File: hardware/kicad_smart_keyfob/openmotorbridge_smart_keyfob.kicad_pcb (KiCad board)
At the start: 2 copper layers, 38 x 19 mm, 25 parts, among them M1 LRA_MOTOR_PADS, SW1 BTN_ARM, SW2 BTN_SOS, U1 nRF52840-QIAA, U2 SX1262IMLTRT, U3 DRV2605LDGSR, U4 BQ51003YFPR, U5 BQ25100YFPR, Y1 32.000MHz, Y2 32.768kHz, Y3 32MHz_TCXO

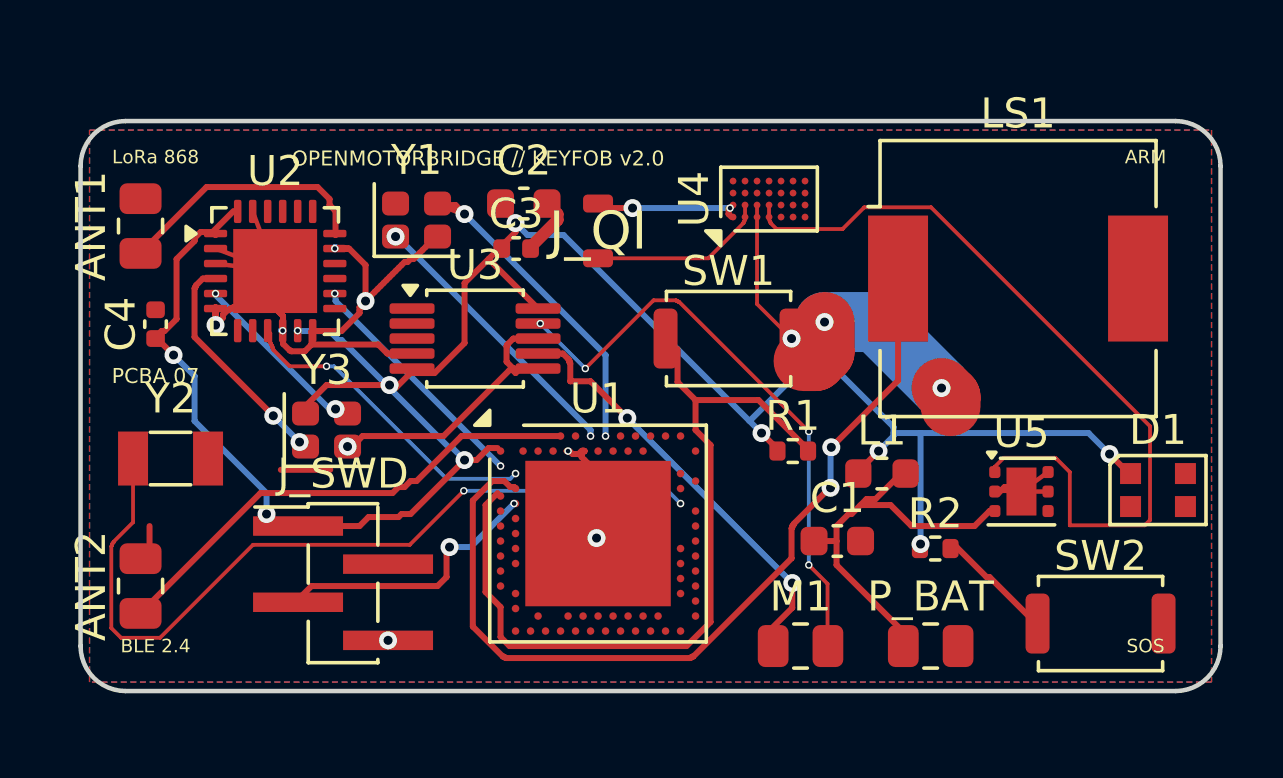
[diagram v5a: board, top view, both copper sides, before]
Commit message: hardware(pcba): commit user manual routing updates for PCBA 07 (keyfob) and PCBA 08 (radar)
- PCBA 07 (Smart Keyfob): 0 unconnected items, complete manual routing of nRF52840, SX1262, Qi charging and power circuits
- PCBA 08 (Radar Sub-MCU): 0 unconnected items, 0 clearance/shorting errors, complete manual routing of MR20 radar interface (TX/RX), ESP32-C5 and power
- Updated high-resolution 3D renders for both boards in hardware/ and docs/images/pcba/
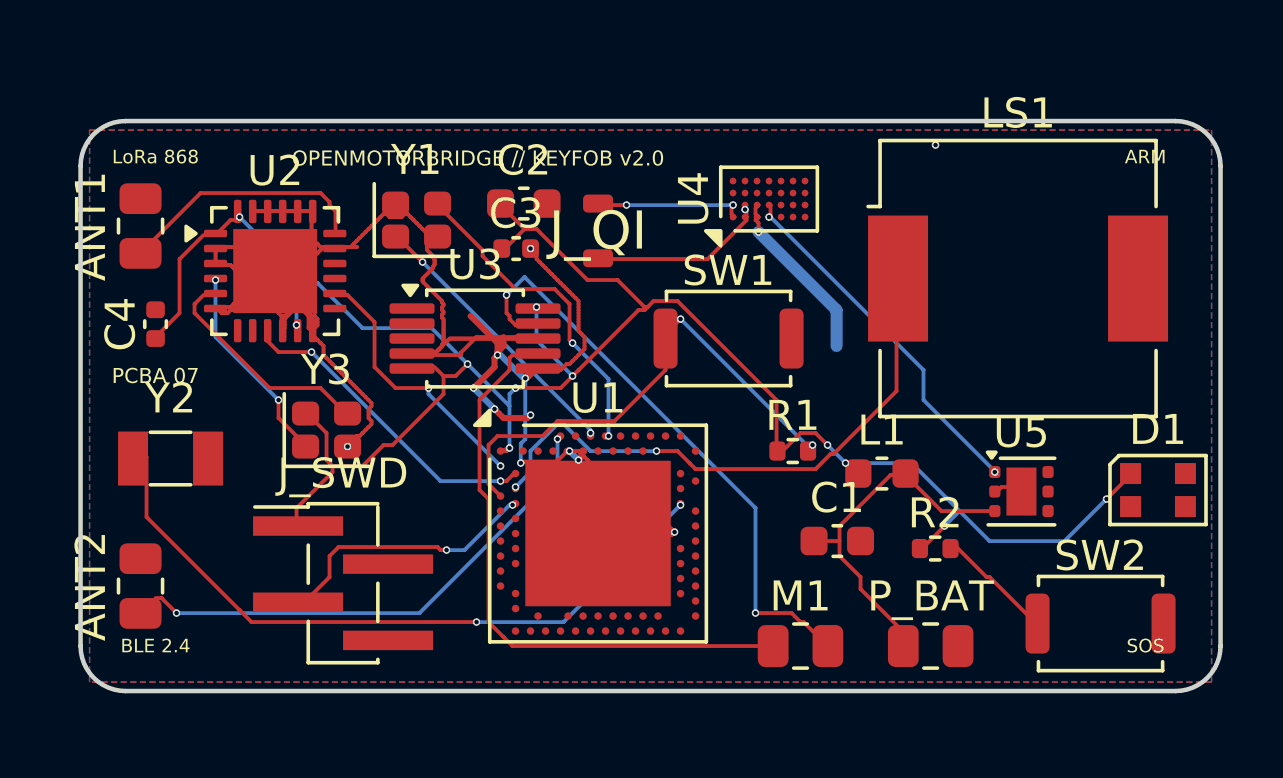
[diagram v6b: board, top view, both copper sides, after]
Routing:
- net GND: track 60.5 -> 88.5 mm, vias 11 -> 13
- net VCC_QI_5V: track 27.3 -> 12.1 mm, vias 0 -> 2
- net BUZZER_PWM: track 29.2 -> 19.6 mm
- net BTN_ARM_N: track 26.7 -> 17.2 mm, vias 0 -> 2
- net LRA_POS: track 14.6 -> 20.2 mm, vias 2 -> 0
- net RTC2: track 27.3 -> 23.3 mm
- net VCC_3V3: track 75.6 -> 73.4 mm, vias 10 -> 11
- net VBAT: track 13.9 -> 12.4 mm
- net TCXO_OUT: track 6.11 -> 7.33 mm, vias 2 -> 0
- net LORA_SCK: track 7.98 -> 8.91 mm
- net TCXO_IN: track 7.65 -> 6.84 mm
- net BLE_ANT_50R: track 16.4 -> 16.9 mm, vias 0 -> 2
- net QI_AC2: track 5.92 -> 6.25 mm, vias 0 -> 1
- net LRA_NEG: track 19.8 -> 20.0 mm, vias 4 -> 2

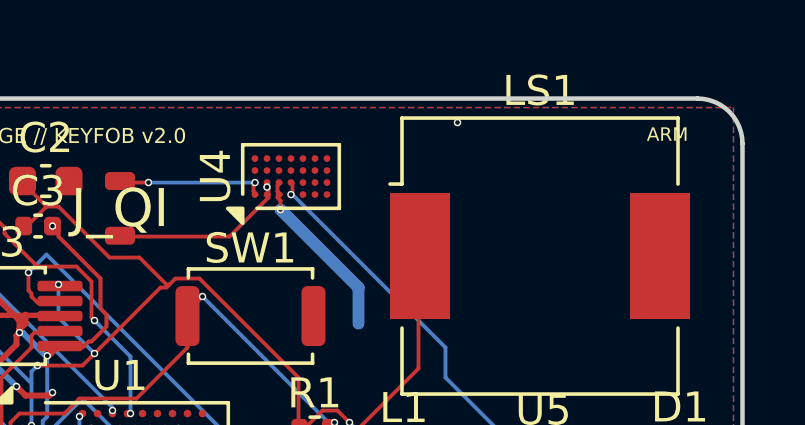
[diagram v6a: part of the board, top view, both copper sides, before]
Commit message: feat(system): architecture refinement v6 across hardware, firmware and docs
- Hardware:
  * PCBA 09 (OMM 2.4 GHz Intercom): Upgrade to Everest Semi ES8388 stereo codec (QFN-28)
    and Multi-Use USB-C connector (J1) combining power, WebUSB flashing and stereo audio.
  * PCBA 08 (Radar 2.0 Sub-MCU): Strict HF hardening (2x U.FL: 6.5 GHz UWB & 5.9 GHz V2X;
    no 2.4 GHz/BLE at rear), right-angle 4-pin flashing header J3.
  * PCBA 03 (Cartridge): 8-pin Kelvin-grounded audio/power header with isolated PGND/AGND.
  * CAD: Standardize DIN 934 hex nut pockets across module enclosures.

- Firmware:
  * UWB Backbone: Add multi-channel substream audio downlink (sub-channels 0/1 music,
    sub-channel 2 voice) and audio uplink packet definitions.
  * Smart Cartridge: Implement zero-latency (<1 ms) voice routing to intercom mic pin,
    A2DP music stream buffering for mesh group sharing, and 100 Hz upstream audio capture.
  * Central Box: Central DSP mixer ducking (-18 dB), voice activity detection (VAD), and
    multi-channel UWB dispatching.
  * OMM Module: Implement ES8388 stereo codec driver and I2S master duplex stream.
  * Radar Sub-MCU: Confirm 2.4 GHz RF disable and autonomous emergency strobe trigger (<1 ms).

- Documentation & WebApp:
  * Align DE & EN chapters (01, 02, 03, 04b, 07, 08, 14, 15, 16) with v6 specifications.
  * Update WebApp PWA System Builder with ES8388 stereo codec and OMM 446 PMR/DMR module.
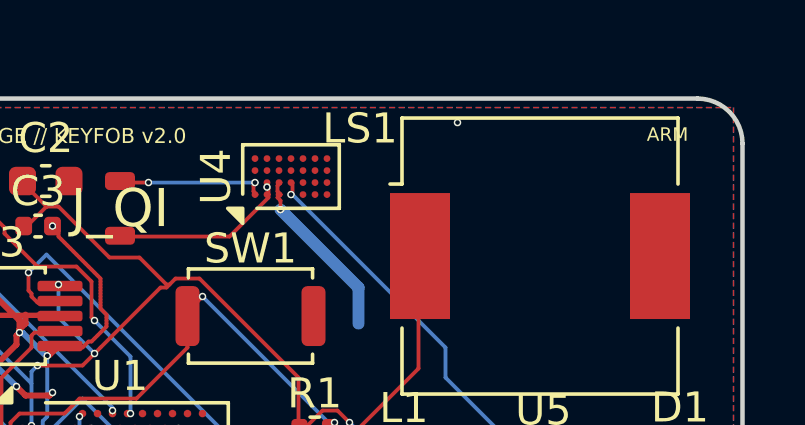
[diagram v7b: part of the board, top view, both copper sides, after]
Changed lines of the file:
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@@
 		(tags "buzzer piezo")
 		(property "Reference" "LS1"
-			(at 0 -5.5 0)
+			(at -6 -4.25 0)
 			(layer "F.SilkS")
 			(effects

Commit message: feat: sync re-routed PCBAs (01, 03, 07, 08, 10), manufacturing packages, 3D renders & docs
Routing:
- net GND: track 88.5 -> 59.8 mm
- net VCC_3V3: track 73.4 -> 71.3 mm
- net BUZZER_PWM: track 19.6 -> 18.5 mm
- net VBAT: track 12.4 -> 11.8 mm
- net QI_AC2: track 6.25 -> 6.09 mm, vias 1 -> 0
